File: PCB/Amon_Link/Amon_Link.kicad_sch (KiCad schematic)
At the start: 103 parts, among them IC1 SPX5205M5-L/TR, J1 USB_C_Receptacle_USB2.0, J2 SMA Edge, J3 Programing port, J4 SMA Edge, SW1 SW_SPST, U1 CH32V003F4P6, U2 CH340G, U3 NRF24L01, U4 RFX2401C, U5 NRF24L01, U6 RFX2401C, Y1 12MHz, Y2 12MHz, Y3 16MHz, Y4 16MHz

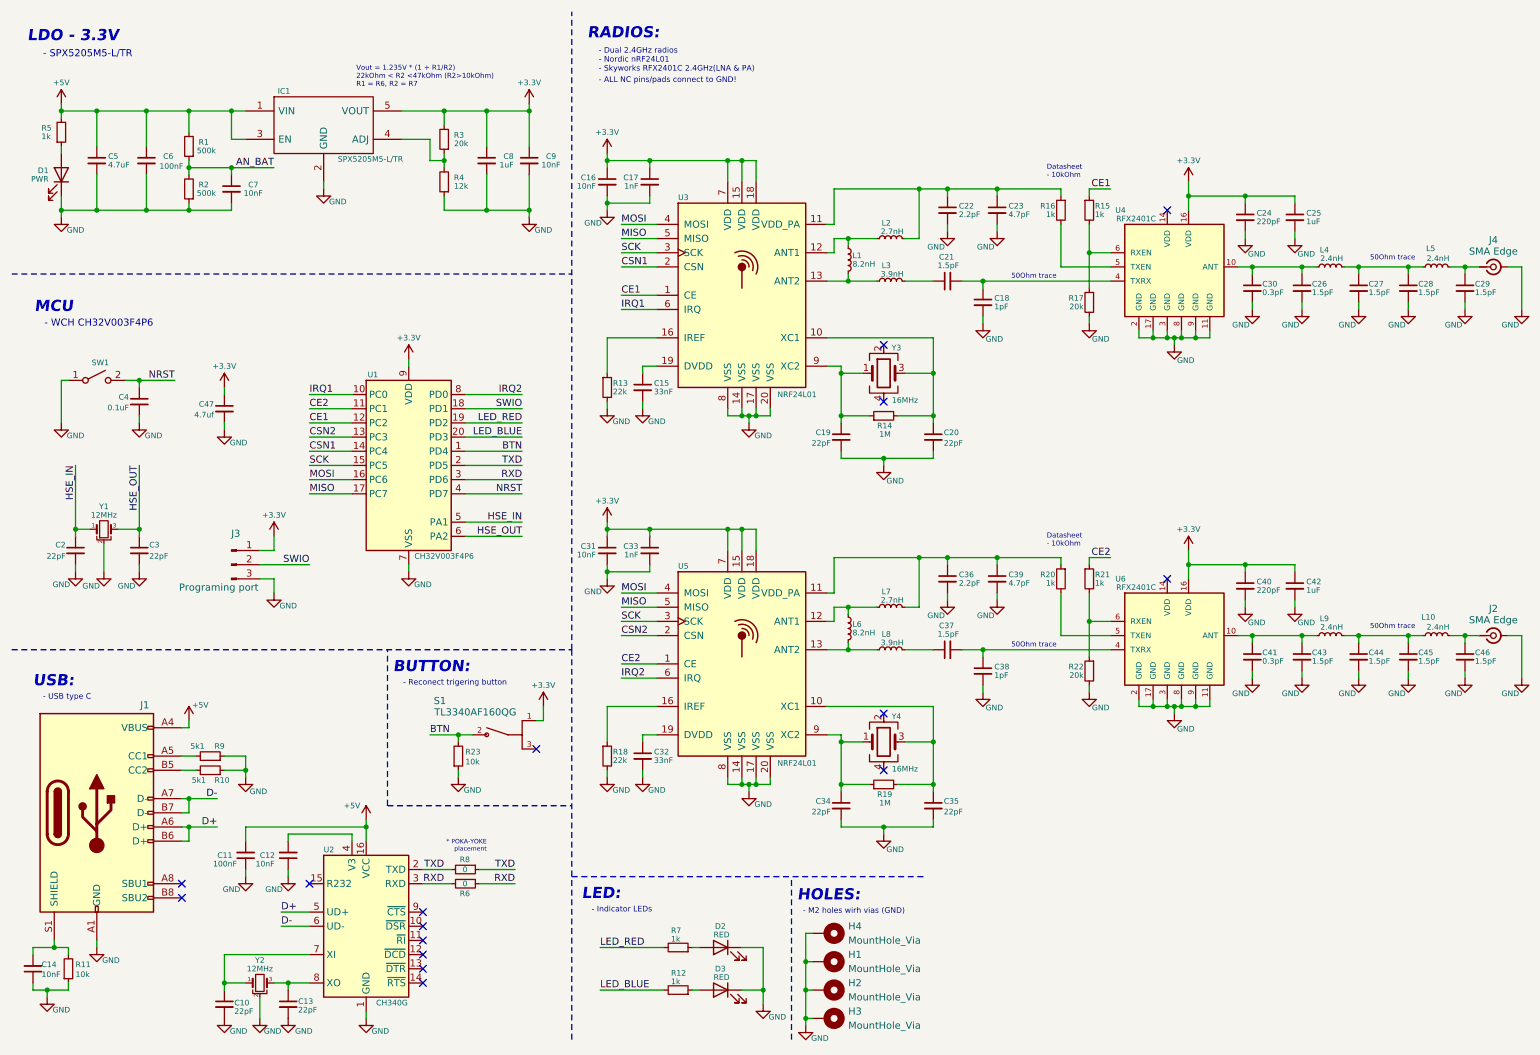
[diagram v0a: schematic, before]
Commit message: shematic done, layout in progress
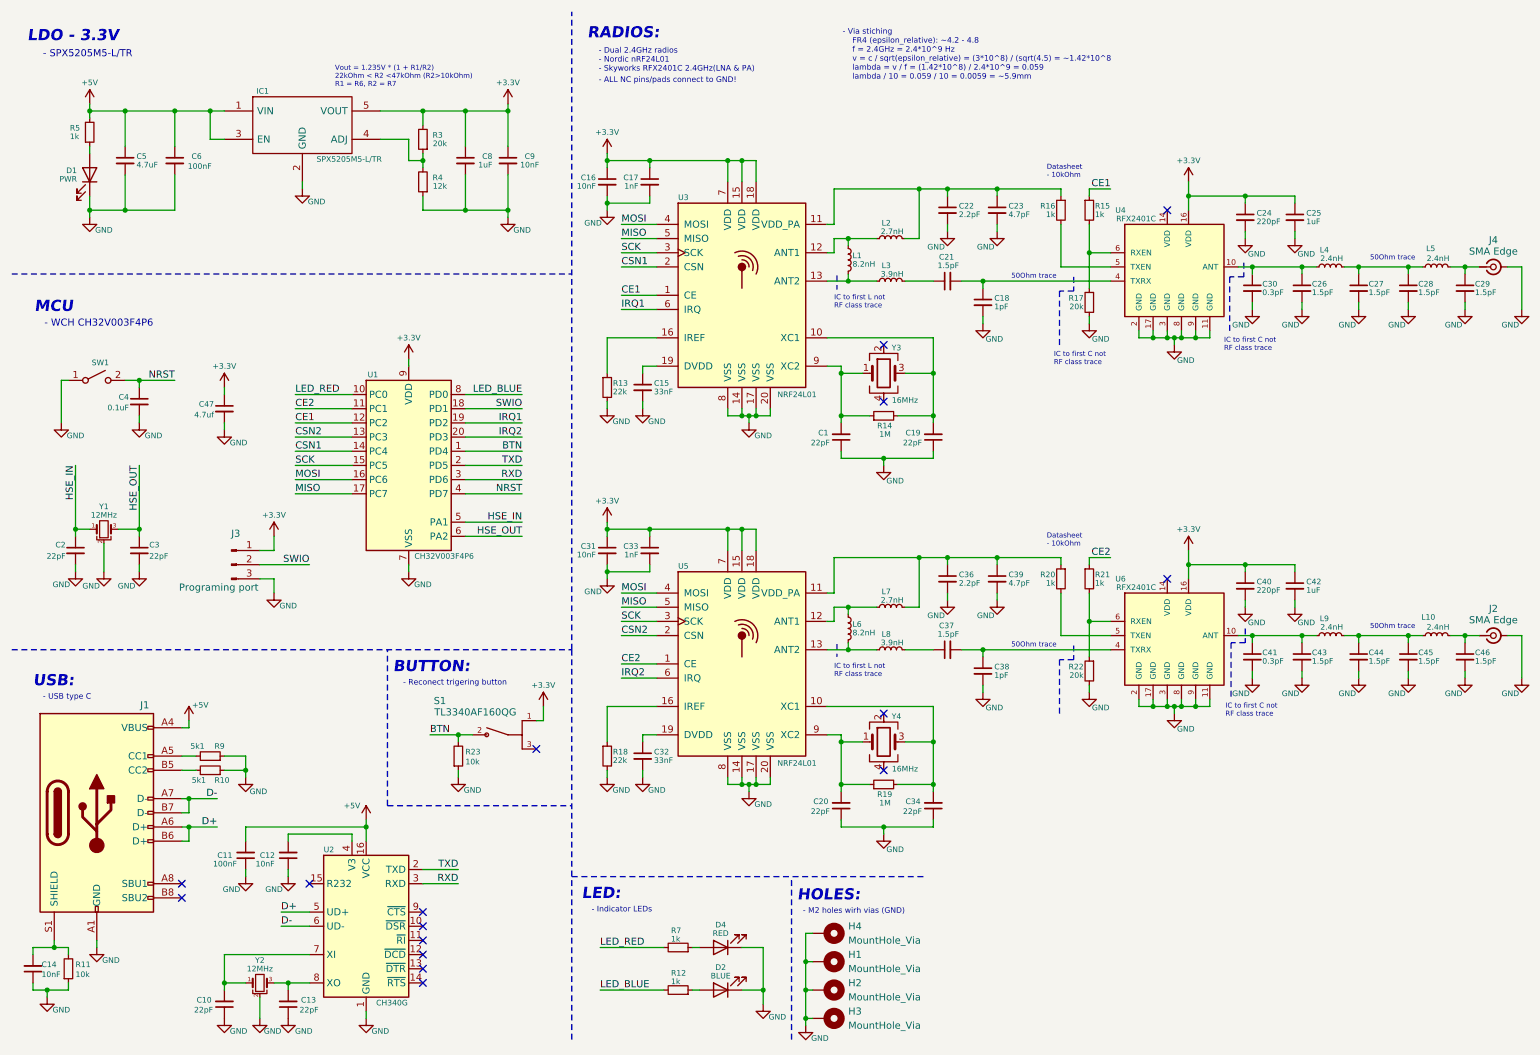
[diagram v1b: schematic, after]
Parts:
- removed C35: 22pF, Capacitor_SMD:C_0603_1608Metric, symbol Device:C_Small
- removed C7: 10nF, Capacitor_SMD:C_0603_1608Metric, symbol Device:C_Small
- removed D3: RED, LED_SMD:LED_0603_1608Metric, symbol Device:LED
- removed R1, R2: 500k, Resistor_SMD:R_0603_1608Metric, symbol Device:R_Small
- removed R6, R8: 0, Resistor_SMD:R_0603_1608Metric, symbol Device:R_Small
- added C1: 22pF, Capacitor_SMD:C_0402_1005Metric, symbol Device:C_Small
- added D4: RED, LED_SMD:LED_1206_3216Metric, symbol Device:LED
- C19, C20, C34: footprint Capacitor_SMD:C_0603_1608Metric -> Capacitor_SMD:C_0402_1005Metric
- D2: value RED -> BLUE; footprint LED_SMD:LED_0603_1608Metric -> LED_SMD:LED_1206_3216Metric
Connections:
- net GND: now also C10.1, C13.1, C19.1, C20.1, C34.1, C1.1, D4.1 (K); no longer C10.2, C13.2, C19.2, C20.2, C34.2
- net IRQ1: now also U1.19 (PD2); no longer U1.10 (PC0)
- net IRQ2: now also U1.20 (PD3); no longer U1.8 (PD0)
- net LED_BLUE: now also U1.8 (PD0); no longer U1.20 (PD3)
- net LED_RED: now also U1.10 (PC0); no longer U1.19 (PD2)
- net at D2.2 (A): now also R12.1; no longer R7.1
- net at R19.1, U5.9 (XC2), Y4.1: now also C20.2; no longer C34.1
- net at R14.2, U3.10 (XC1), Y3.3: now also C19.2; no longer C20.1
- net at R19.2, U5.10 (XC1), Y4.3: now also C34.2
- net at U2.7 (XI), Y2.1: now also C10.2; no longer C10.1
- net at R14.1, U3.9 (XC2), Y3.1: now also C1.2; no longer C19.1
- net at U2.8 (XO), Y2.3: now also C13.2; no longer C13.1
- new net: D4.2 (A), R7.1
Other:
- note added: "- Via stiching FR4 (epsilon_relative): ~4.2 - 4.8 f = 2.4GHz = 2.4*10^9 Hz v = c / sqrt(epsilon_relative) = (3*10^8) / (sqrt(4.5) = ~1.42*10^8 lambda = v / f = (1.42*10^8) / 2.4*10^9 = 0.059 lambda / 10 = 0.059 / 10 = 0.0059 = ~5.9mm"
- note added: "IC to first C not RF class trace"
- note added: "IC to first L not RF class trace"
- note removed: "* POKA-YOKE placement"
- moved on the sheet: C5, C6, C8, C9, D1, IC1, R3, R4, R5

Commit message: pcb update and case
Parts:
- added R1, R2: 10k, Resistor_SMD:R_0603_1608Metric, symbol Device:R_Small
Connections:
- net +3.3V: now also R1.2, R2.2
- net CE1: now also U1.13 (PC3); no longer U1.12 (PC2)
- net CE2: now also U1.12 (PC2); no longer U1.11 (PC1)
- net CSN1: now also R2.1
- net CSN2: now also U1.19 (PD2), R1.1; no longer U1.13 (PC3)
- net IRQ1: now also U1.20 (PD3); no longer U1.19 (PD2)
- net IRQ2: now also U1.11 (PC1); no longer U1.20 (PD3)
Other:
- moved on the sheet: C4, C47, SW1, U1

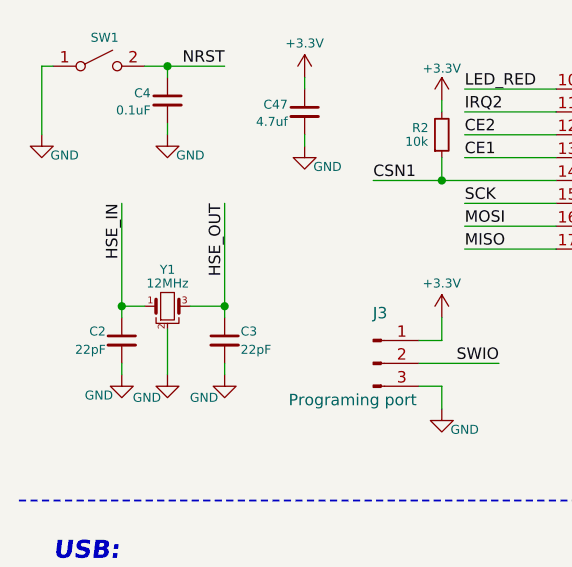
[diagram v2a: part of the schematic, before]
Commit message: PCB: added graphics, Firmware: USART IRQ working, pinout set
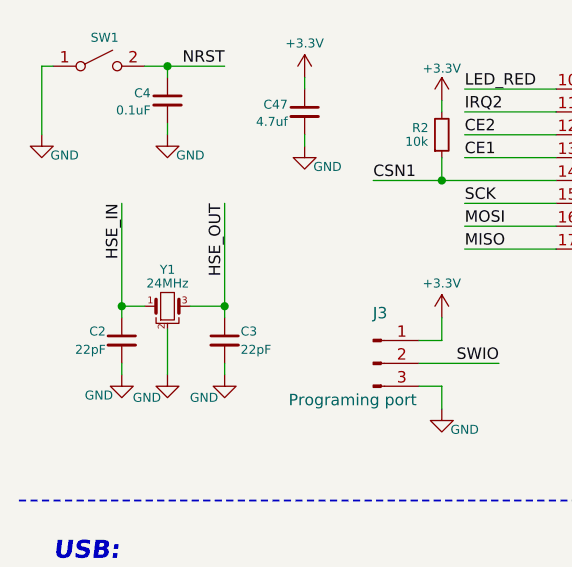
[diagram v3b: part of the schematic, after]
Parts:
- Y1: value 12MHz -> 24MHz
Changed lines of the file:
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@@
 			)
 		)
-		(property "Value" "12MHz"
+		(property "Value" "24MHz"
 			(at 29.21 102.87 0)
 			(effects

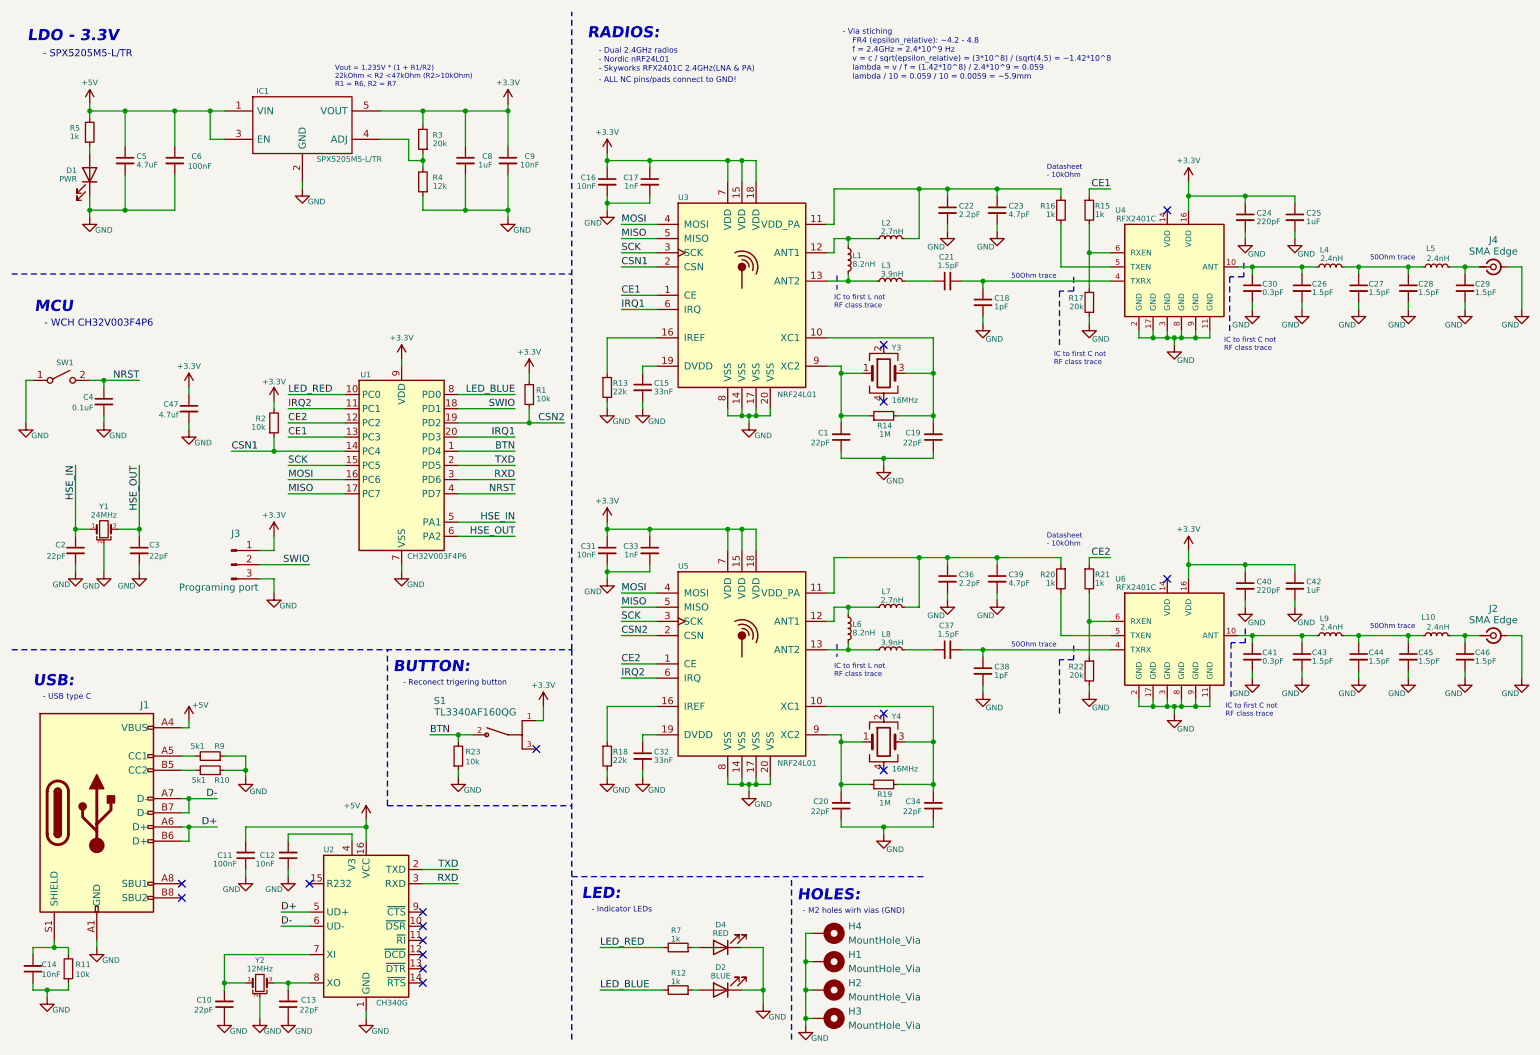
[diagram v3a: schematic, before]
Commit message: Update
PCB v0.1 complete, firmware in progress
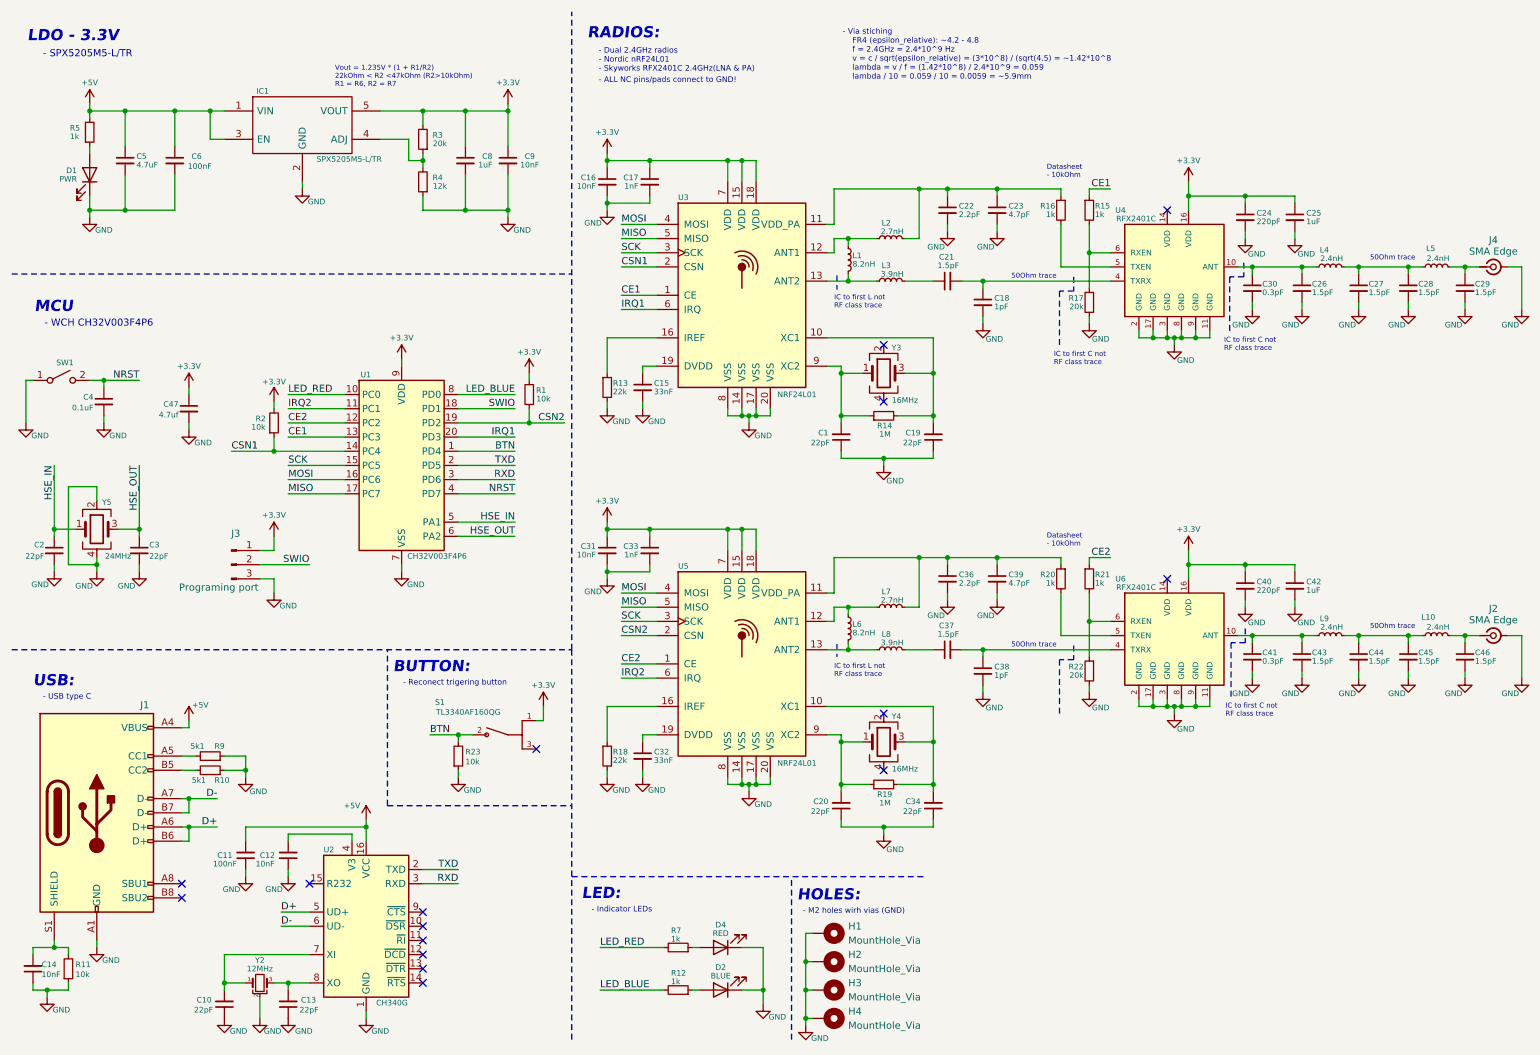
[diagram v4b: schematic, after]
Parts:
- removed Y1: 24MHz, Crystal:Resonator_SMD_Murata_CSTxExxV-3Pin_3.0x1.1mm, symbol Device:Crystal_GND2_Small
- added Y5: 24MHz, Crystal:Crystal_SMD_3225-4Pin_3.2x2.5mm, symbol Device:Crystal_GND24
- H1, H2, H3, H4: now left out of the parts list
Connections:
- net GND: now also Y5.2, Y5.4
- net HSE_IN: now also Y5.1
- net HSE_OUT: now also Y5.3
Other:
- moved on the sheet: C2
